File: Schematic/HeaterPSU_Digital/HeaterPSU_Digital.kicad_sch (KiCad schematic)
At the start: 75 parts, among them J1 SMPS2_SEC, J2 Heater output, J3 Conn_01x06, Q1 IRF4905, Q2 SIRA24DP, U1 XL4005, U2 ADA4522-2, U3 MCP4726, U4 TPS54302, U5 INA293B1QDBVRQ1, U6 MCP4726, U7 INA219AIDCNR

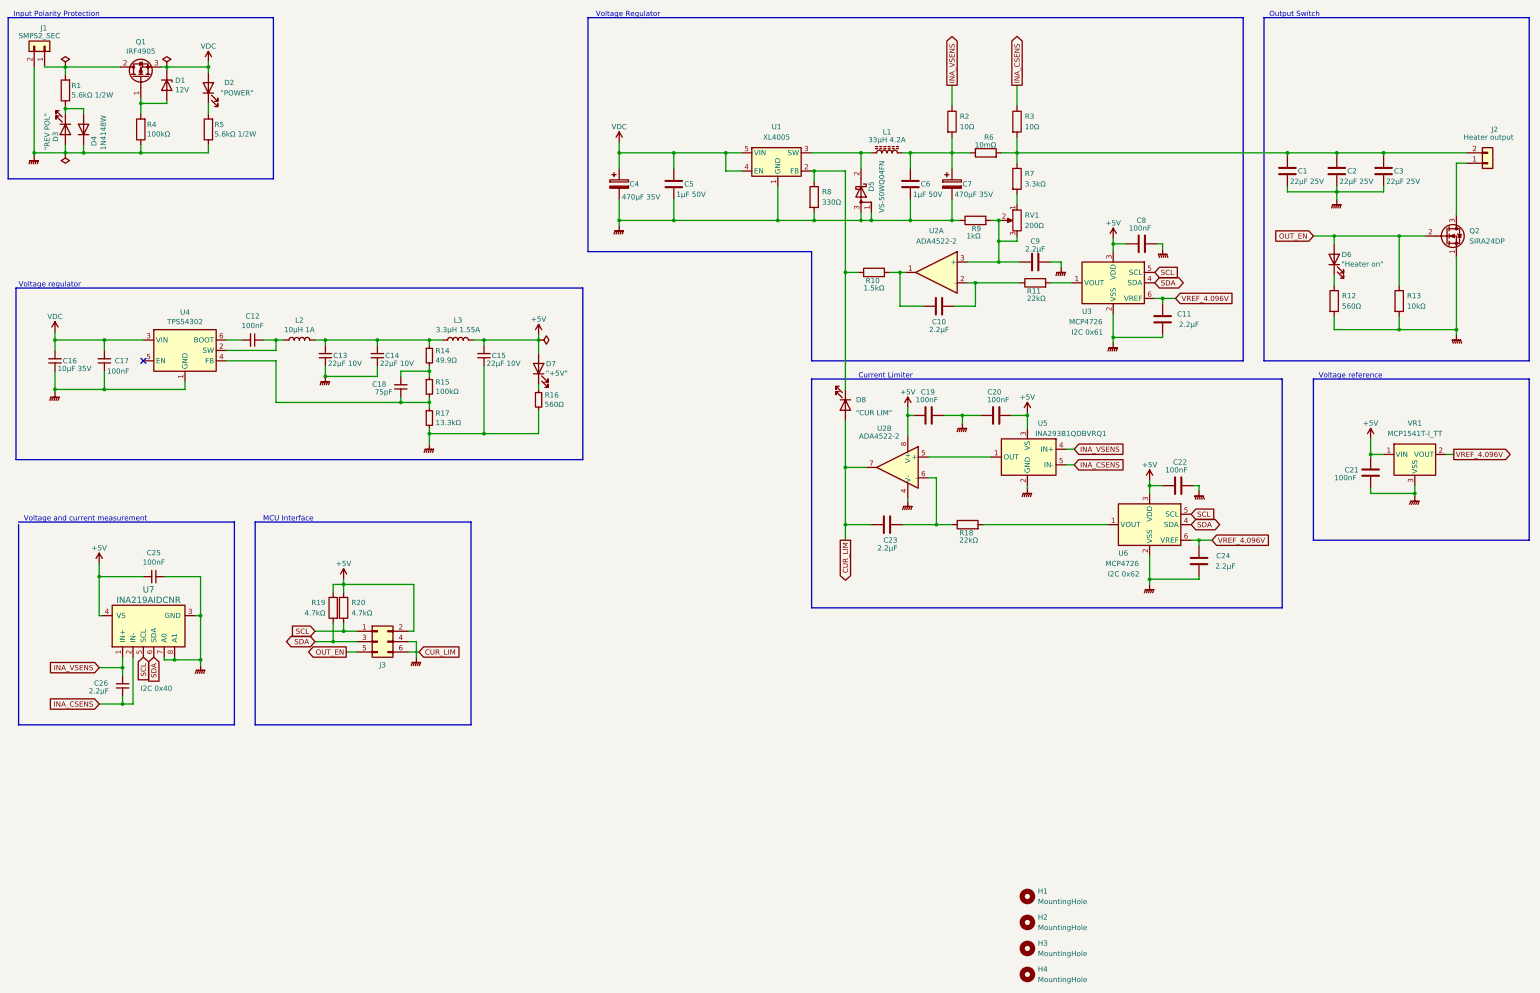
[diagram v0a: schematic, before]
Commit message: Added driver stage for output MOSFET
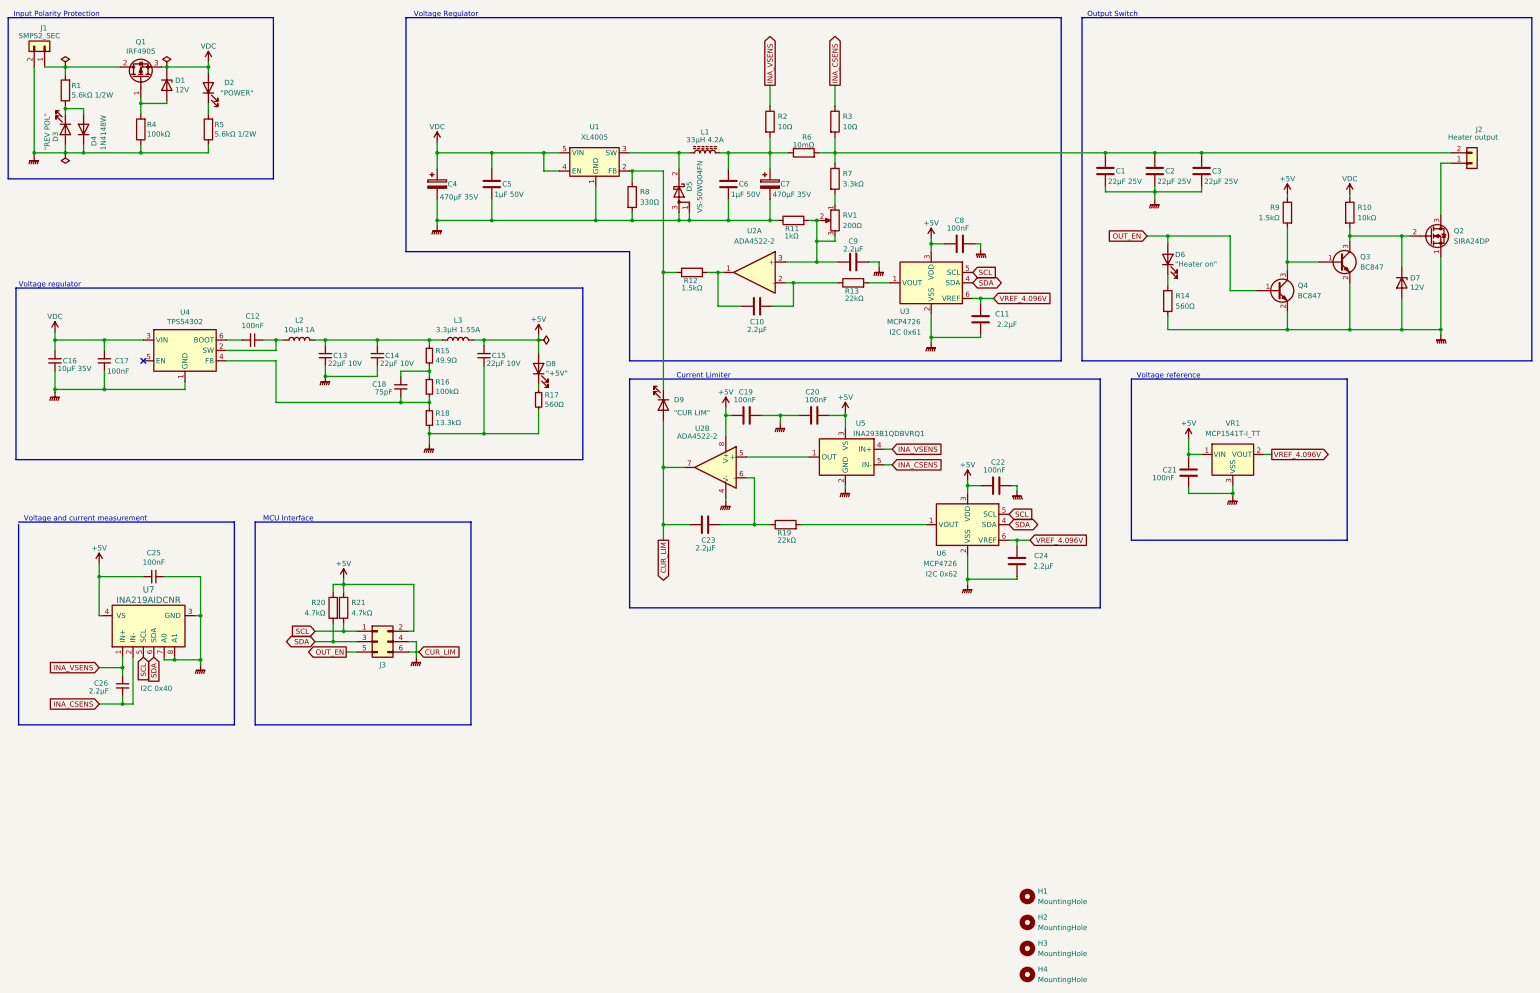
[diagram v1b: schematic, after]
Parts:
- added D7: 12V, Diode_SMD:D_SOD-123, symbol Device:D_Zener
- added Q3, Q4: BC847, Package_TO_SOT_SMD:SOT-23, symbol Transistor_BJT:BC847
- added R9: 1.5kΩ, Resistor_SMD:R_0603_1608Metric_Pad0.98x0.95mm_HandSolder, symbol Device:R
- renumbered D7 to D8, D8 to D9, R13 to R10, R9 to R11, R10 to R12, R11 to R13, R12 to R14, R14 to R15, R15 to R16, R16 to R17, R17 to R18, R18 to R19, R19 to R20, R20 to R21
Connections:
- net +5V: now also R9.1
- net GNDPWR: now also D7.2 (A), Q3.2 (E), Q4.2 (E); no longer R10.2
- net OUT_EN: now also Q4.1 (B); no longer Q2.2 (G), R10.1
- net VDC: now also R10.1
- new net: Q3.1 (B), Q4.3 (C), R9.2
- new net: D7.1 (K), Q2.2 (G), Q3.3 (C), R10.2
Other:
- moved on the sheet: C1, C10, C11, C19, C2, C20, C21, C22, C23, C24, C3, C4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
